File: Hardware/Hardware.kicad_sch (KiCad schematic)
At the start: 42 parts, among them J1 ILI9341, J2 RJ45_LED_Shielded, SW1 SW_SPST, SW10 SW_Push, SW11 SW_Push, SW12 SW_Push, SW13 SW_Push, SW2 SW_Push, SW3 SW_Push, SW4 SW_Push, SW5 SW_Push, SW6 SW_Push, SW7 SW_Push, SW8 SW_Push, SW9 SW_Push, U1 TMR-0511, U2 ATA6561, U3 Teensy4.1_DEV-16771

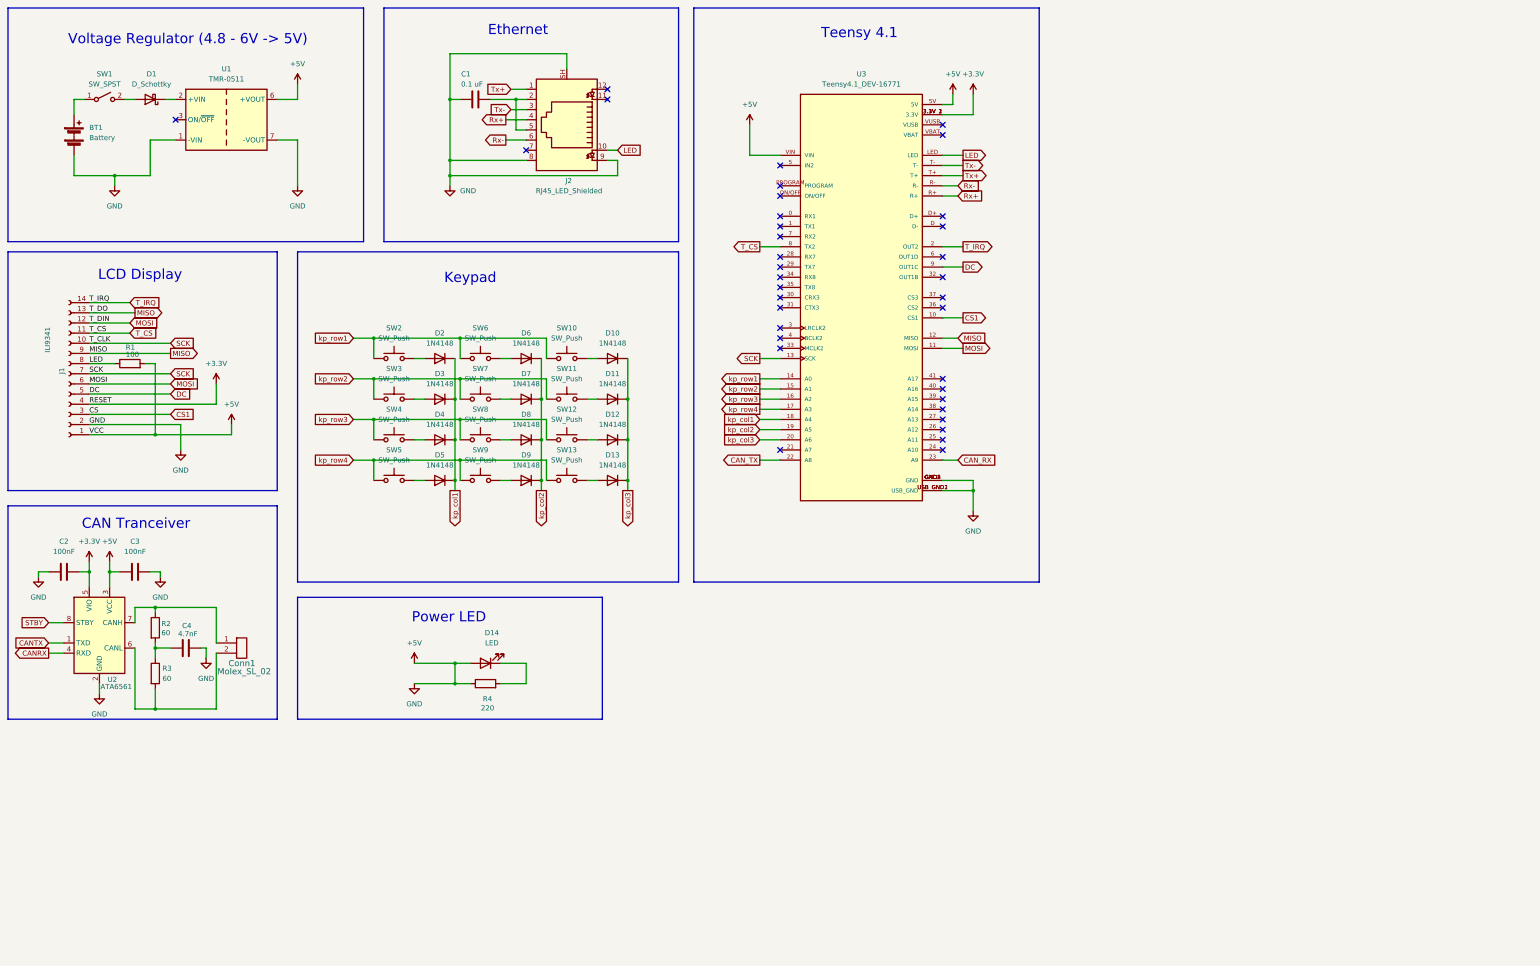
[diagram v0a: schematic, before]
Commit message: added usb port and wifi module
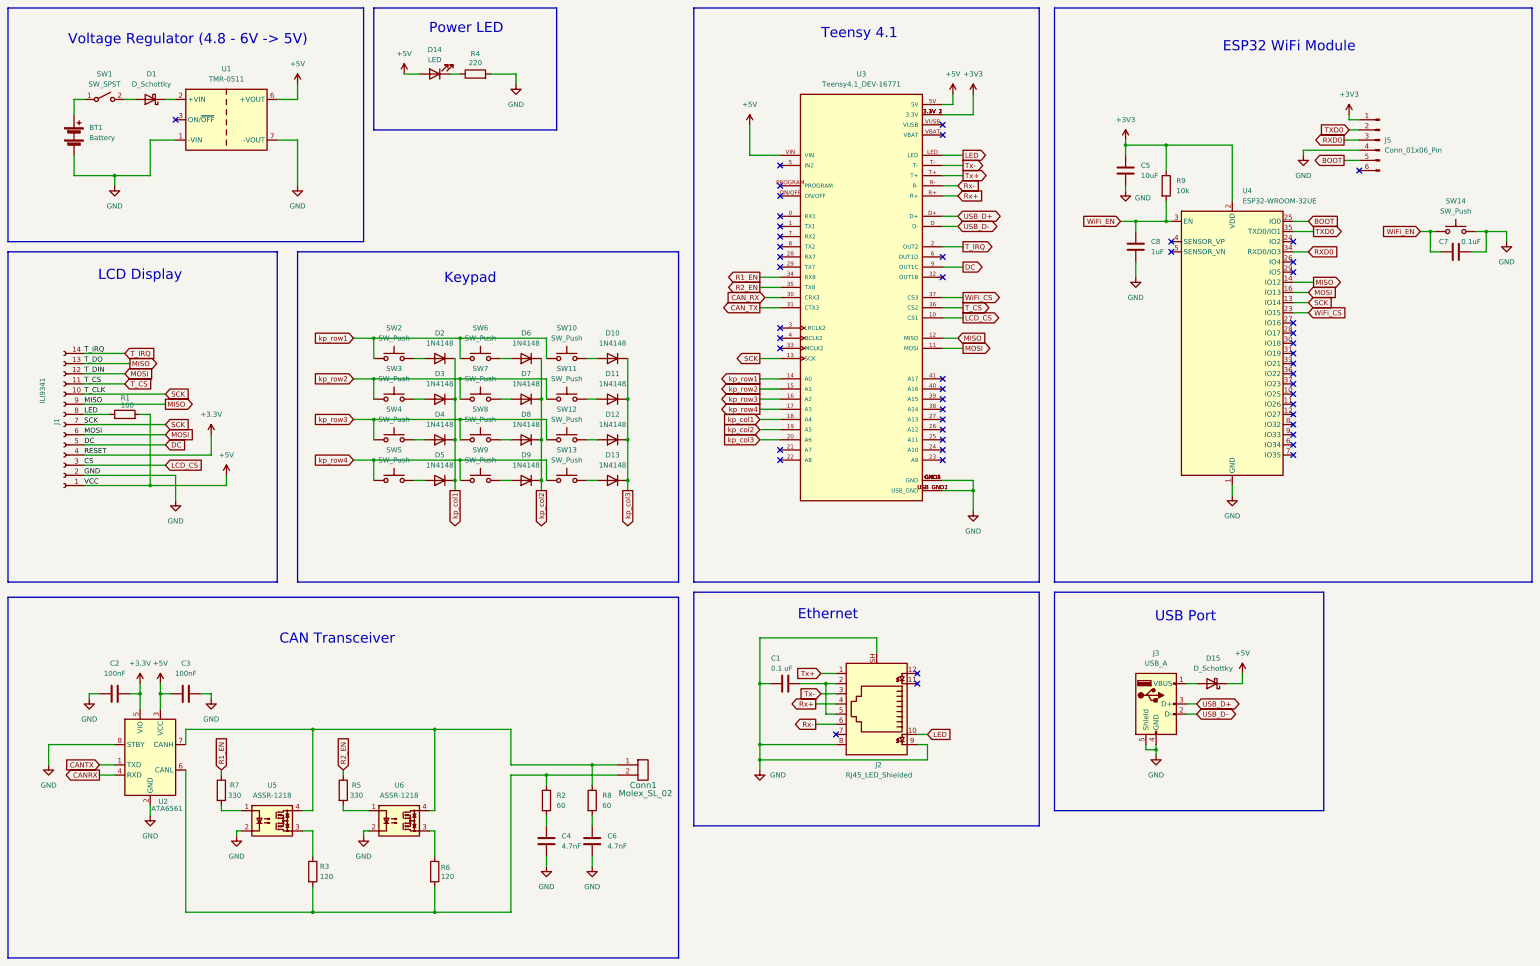
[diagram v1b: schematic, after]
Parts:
- added C5: 10uF, symbol Device:C
- added C6: 4.7nF, symbol Device:C
- added C7: 0.1uF, symbol Device:C
- added C8: 1uF, symbol Device:C
- added D15: D_Schottky, symbol Device:D_Schottky
- added J3: USB_A, Connector_USB:USB_A_Molex_67643_Horizontal, symbol Connector:USB_A
- added J5: Conn_01x06_Pin, symbol Connector:Conn_01x06_Pin
- added R5, R7: 330, symbol Device:R
- added R6: 120, Resistor_SMD:R_0603_1608Metric_Pad0.98x0.95mm_HandSolder, symbol Device:R
- added R8: 60, symbol Device:R
- added R9: 10k, symbol Device:R
- added SW14: SW_Push, symbol Switch:SW_Push
- added U4: ESP32-WROOM-32UE, RF_Module:ESP32-WROOM-32UE, symbol RF_Module:ESP32-WROOM-32UE
- added U5, U6: ASSR-1218, Package_SO:SO-4_4.4x4.3mm_P2.54mm, symbol Relay_SolidState:ASSR-1218
- R2: footprint Resistor_SMD:R_0603_1608Metric_Pad0.98x0.95mm_HandSolder -> (none)
- R3: value 60 -> 120
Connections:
- net +3.3V: no longer U3.3.3V_1 (3.3V), U3.3.3V_2 (3.3V), U3.3.3V_3 (3.3V)
- net +5V: now also D15.1 (K); no longer BT1.2 (-), C1.2, C2.2, C3.2, C4.2, J1.2 (Pin_2), J2.8, J2.9, J2.SH, R4.1, U1.1 (-VIN), U1.7 (-VOUT), U2.2 (GND), U3.GND1 (GND), U3.GND2 (GND), U3.GND3 (GND), U3.GND4 (GND), U3.GND5 (GND), U3.USB_GND1 (USB_GND), U3.USB_GND2 (USB_GND)
- net CAN_RX: now also U3.30 (CRX3); no longer U3.23 (A9)
- net CAN_TX: now also U3.31 (CTX3); no longer U3.22 (A8)
- net MISO: now also U4.14 (IO12)
- net MOSI: now also U4.16 (IO13)
- net SCK: now also U4.13 (IO14)
- net T_CS: now also U3.36 (CS2); no longer U3.8 (TX2)
- net at D14.1 (K): now also R4.1; no longer R4.2
- net at Conn1.1, U2.7 (CANH): now also R8.1, U5.4, U6.4; no longer R2.1
- net at C4.1, R2.2: no longer R3.1
- net at Conn1.2, R3.2, U2.6 (CANL): now also R2.1, R6.2
- net R1_EN: now reaches U3.34 (RX8)
- net R1_EN: now also R7.1
- net R2_EN: now reaches U3.35 (TX8)
- net R2_EN: now also R5.1
- net WiFi_CS: now reaches U3.37 (CS3)
- net WiFi_CS: now also U4.23 (IO15)
- net USB_D-: now reaches U3.D (D-)
- net USB_D-: now also J3.2 (D-)
- net USB_D+: now reaches U3.D+
- net USB_D+: now also J3.3 (D+)
- net CS1 renamed LCD_CS
- net STBY renamed GND
- net GND: now also BT1.2 (-), C1.2, C2.2, C3.2, C4.2, J1.2 (Pin_2), J2.8, J2.9, J2.SH, R4.2, U1.1 (-VIN), U1.7 (-VOUT), U2.2 (GND), U3.GND1 (GND), U3.GND2 (GND), U3.GND3 (GND), U3.GND4 (GND), U3.GND5 (GND), U3.USB_GND1 (USB_GND), U3.USB_GND2 (USB_GND), C5.2, C6.2, C7.2, C8.2, J3.4 (GND), J3.5 (Shield), J5.4 (Pin_4), SW14.2, U4.1 (GND), U4.15 (GND), U4.38 (GND), U4.39 (GND), U5.2, U6.2
- new net: C6.1, R8.2
- new net: R6.1, U6.3
- new net: R5.2, U6.1
- new net: D15.2 (A), J3.1 (VBUS)
- new net: R7.2, U5.1
- new net: R3.1, U5.3
- new net +3V3: C5.1, J5.1 (Pin_1), R9.1, U3.3.3V_1 (3.3V), U3.3.3V_2 (3.3V), U3.3.3V_3 (3.3V), U4.2 (VDD)
- new net BOOT: J5.5 (Pin_5), U4.25 (IO0)
- new net RXD0: J5.3 (Pin_3), U4.34 (RXD0/IO3)
- new net TXD0: J5.2 (Pin_2), U4.35 (TXD0/IO1)
- new net WiFi_EN: C7.1, C8.1, R9.2, SW14.1, U4.3 (EN)
- no-connect marks 36 -> 51
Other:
- note added: "CAN Transceiver"
- note added: "ESP32 WiFi Module"
- note added: "USB Port"
- note removed: "CAN Tranceiver"
- moved on the sheet: C1, C2, C3, Conn1, D14, J1, J2, R1, R3, R4, U2

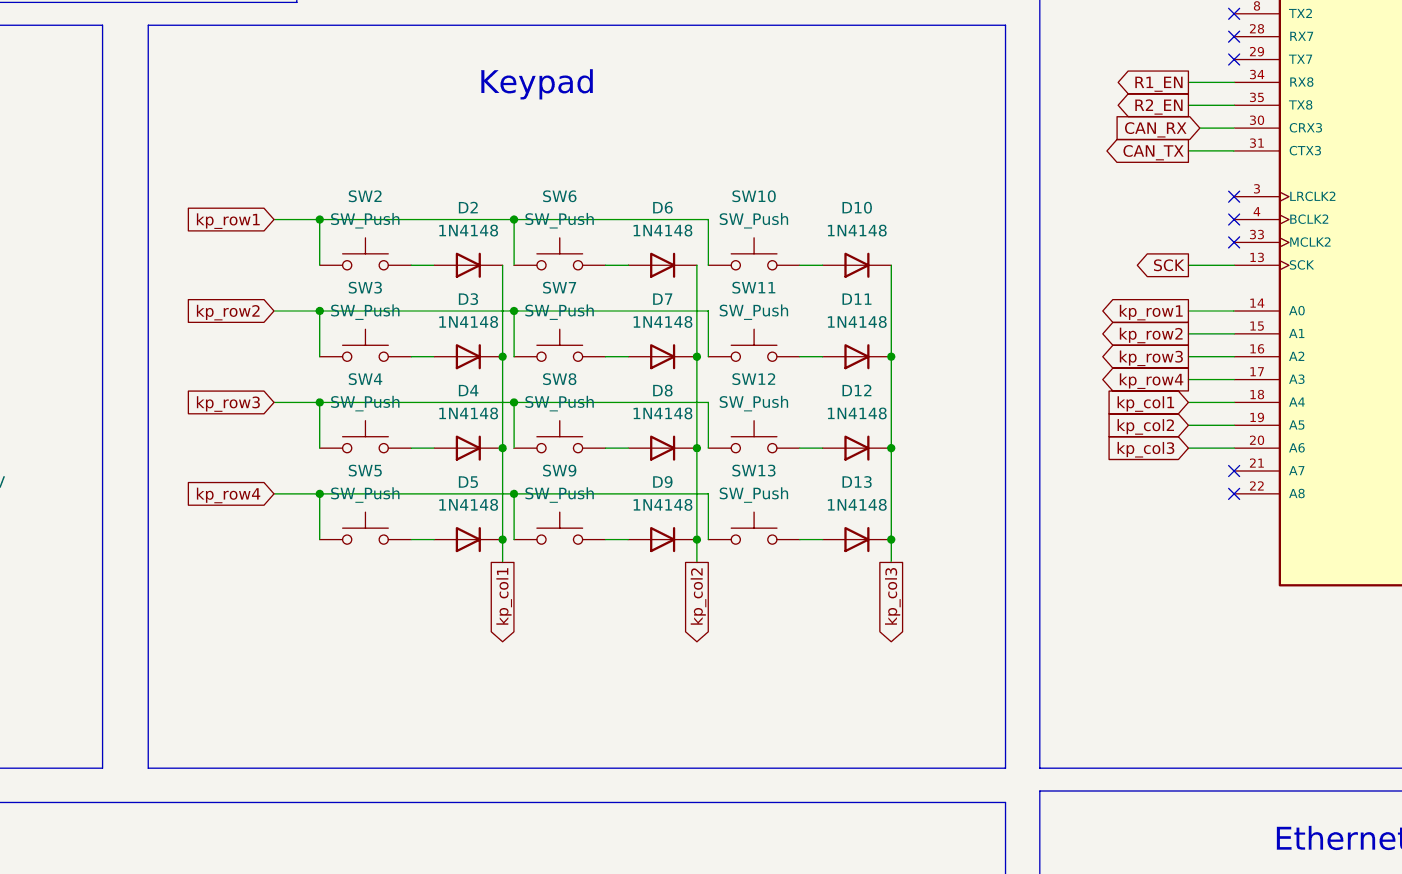
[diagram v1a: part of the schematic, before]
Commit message: fixed schematic for layout
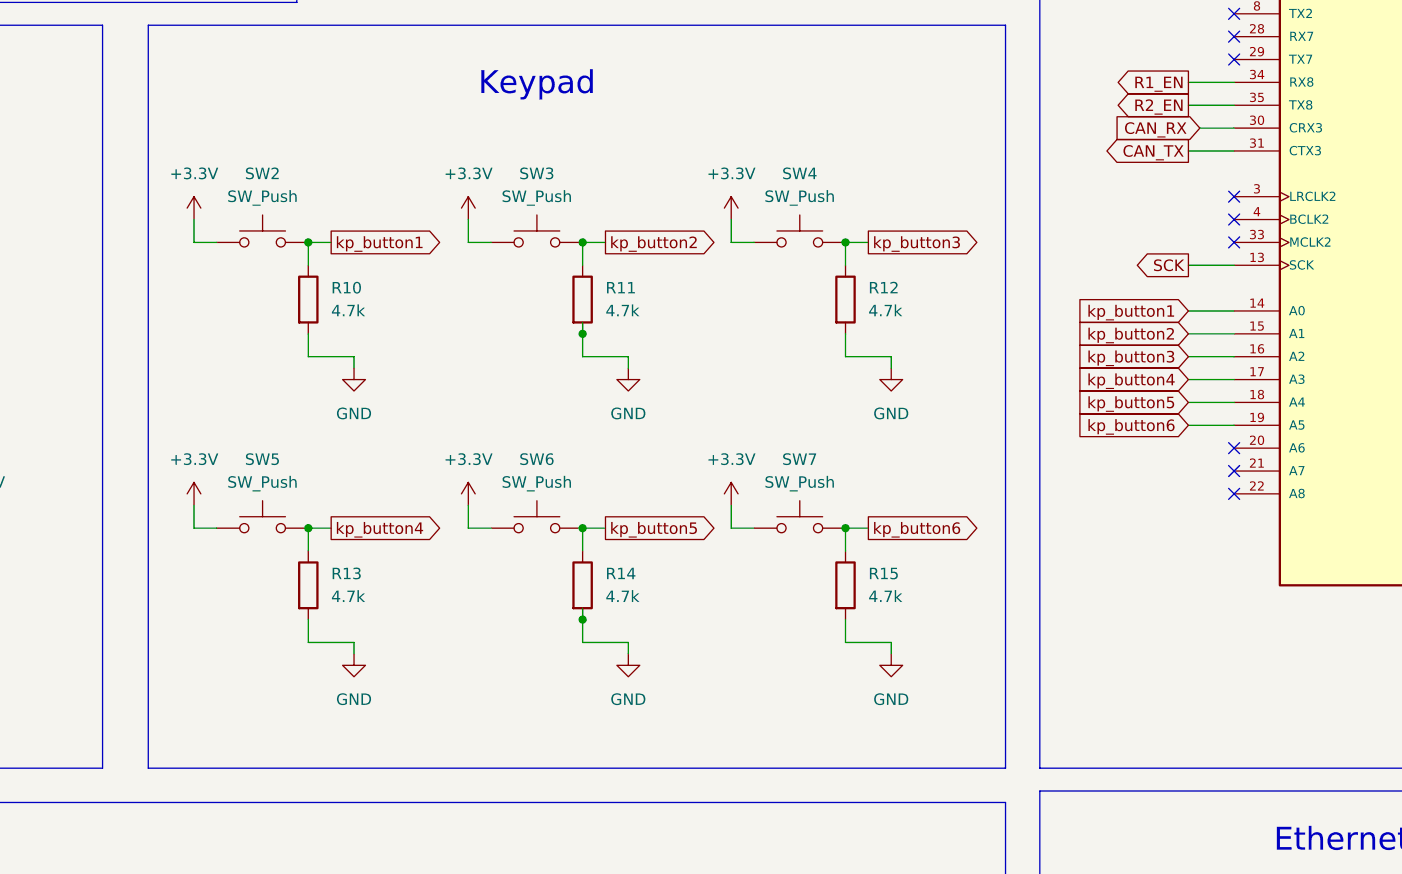
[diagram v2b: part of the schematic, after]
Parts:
- removed D10, D11, D12, D13, D2, D3, D4, D5, D6, D7, D8, D9: 1N4148, Diode_THT:D_DO-35_SOD27_P7.62mm_Horizontal, symbol Diode:1N4148
- removed SW10, SW11, SW12, SW13, SW8, SW9: SW_Push, symbol Switch:SW_Push
- added R10, R11, R12, R13, R14, R15: 4.7k, Resistor_SMD:R_0603_1608Metric_Pad0.98x0.95mm_HandSolder, symbol Device:R
- BT1: footprint (none) -> Connector_Wire:SolderWire-0.15sqmm_1x02_P4mm_D0.5mm_OD1.5mm_Relief
- C1, C2, C3, C4, C5, C6, C7, C8: footprint (none) -> Capacitor_SMD:C_0603_1608Metric_Pad1.08x0.95mm_HandSolder
- Conn1: footprint (none) -> MRDT_Connectors:MOLEX_SL_02_Vertical
- D1, D15: footprint (none) -> MRDT_Passives:SOT-23_Diode
- D14: footprint (none) -> LED_SMD:LED_0603_1608Metric_Pad1.05x0.95mm_HandSolder
- J1: footprint (none) -> Connector_PinSocket_2.54mm:PinSocket_1x14_P2.54mm_Vertical
- J2: footprint (none) -> MRDT_Connectors:RJ45_Teensy
- J5: footprint (none) -> Connector_PinHeader_2.54mm:PinHeader_1x06_P2.54mm_Vertical
- R2, R5, R7, R8, R9: footprint (none) -> Resistor_SMD:R_0603_1608Metric_Pad0.98x0.95mm_HandSolder
- SW1: footprint (none) -> sw_spst:SOIC450P1000X730-4N
- SW14, SW2, SW3, SW4, SW5, SW6, SW7: footprint (none) -> Button_Switch_SMD:SW_SPST_TL3305A
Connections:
- net kp_col1 is gone; now on net kp_button5: U3.18 (A4)
- net kp_col2 is gone; now on net kp_button6: U3.19 (A5)
- net +3.3V: now also SW2.1, SW3.1, SW4.1, SW5.1, SW6.1, SW7.1
- net GND: now also R10.2, R11.2, R12.2, R13.2, R14.2, R15.2
- net kp_button4: now reaches SW5.2
- net kp_button4: now also U3.17 (A3), R13.1
- net kp_button5: now reaches SW6.2
- net kp_button5: now also R14.1
- net kp_button6: now reaches SW7.2
- net kp_button6: now also R15.1
- net kp_button3: now reaches SW4.2
- net kp_button3: now also U3.16 (A2), R12.1
- net kp_button2: now reaches SW3.2
- net kp_button2: now also U3.15 (A1), R11.1
- net kp_button1: now reaches SW2.2
- net kp_button1: now also U3.14 (A0), R10.1
- net kp_col3: no longer names the net of U3.20 (A6)
- removed net kp_row1: SW2.1, SW6.1, U3.14 (A0)
- removed net kp_row2: SW3.1, SW7.1, U3.15 (A1)
- removed net kp_row3: SW4.1, U3.16 (A2)
- removed net kp_row4: SW5.1, U3.17 (A3)
- no-connect marks 51 -> 52
